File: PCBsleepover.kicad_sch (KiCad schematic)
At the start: 0 parts

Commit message: worked on sch
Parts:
- added BT1: Battery, symbol Device:Battery
- added C1: C_Polarized, symbol Device:C_Polarized
- added D1: LED, symbol Device:LED
- added R1, R2: R, symbol Device:R
- added R3: R_Variable, symbol Device:R_Variable
- added SW1: SW_Push, symbol Switch:SW_Push
- added U1: ICM7555xB, Package_SO:SOIC-8_3.9x4.9mm_P1.27mm, symbol Timer:ICM7555xB
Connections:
- new net: C1.1, R2.1, U1.2 (TRIG), U1.6 (THRES)
- new net: BT1.2 (-), SW1.2
- new net: R1.1, U1.3 (OUT)
- new net: R3.2, SW1.1, U1.4 (~{RST}), U1.8 (VCC)
- new net: R2.2, R3.1, U1.7 (DISCH)
- new net GND: BT1.1 (+), C1.2, D1.1 (K), U1.1 (GND)
- new net TOUT: D1.2 (A), R1.2
- no-connect marks 0 -> 1

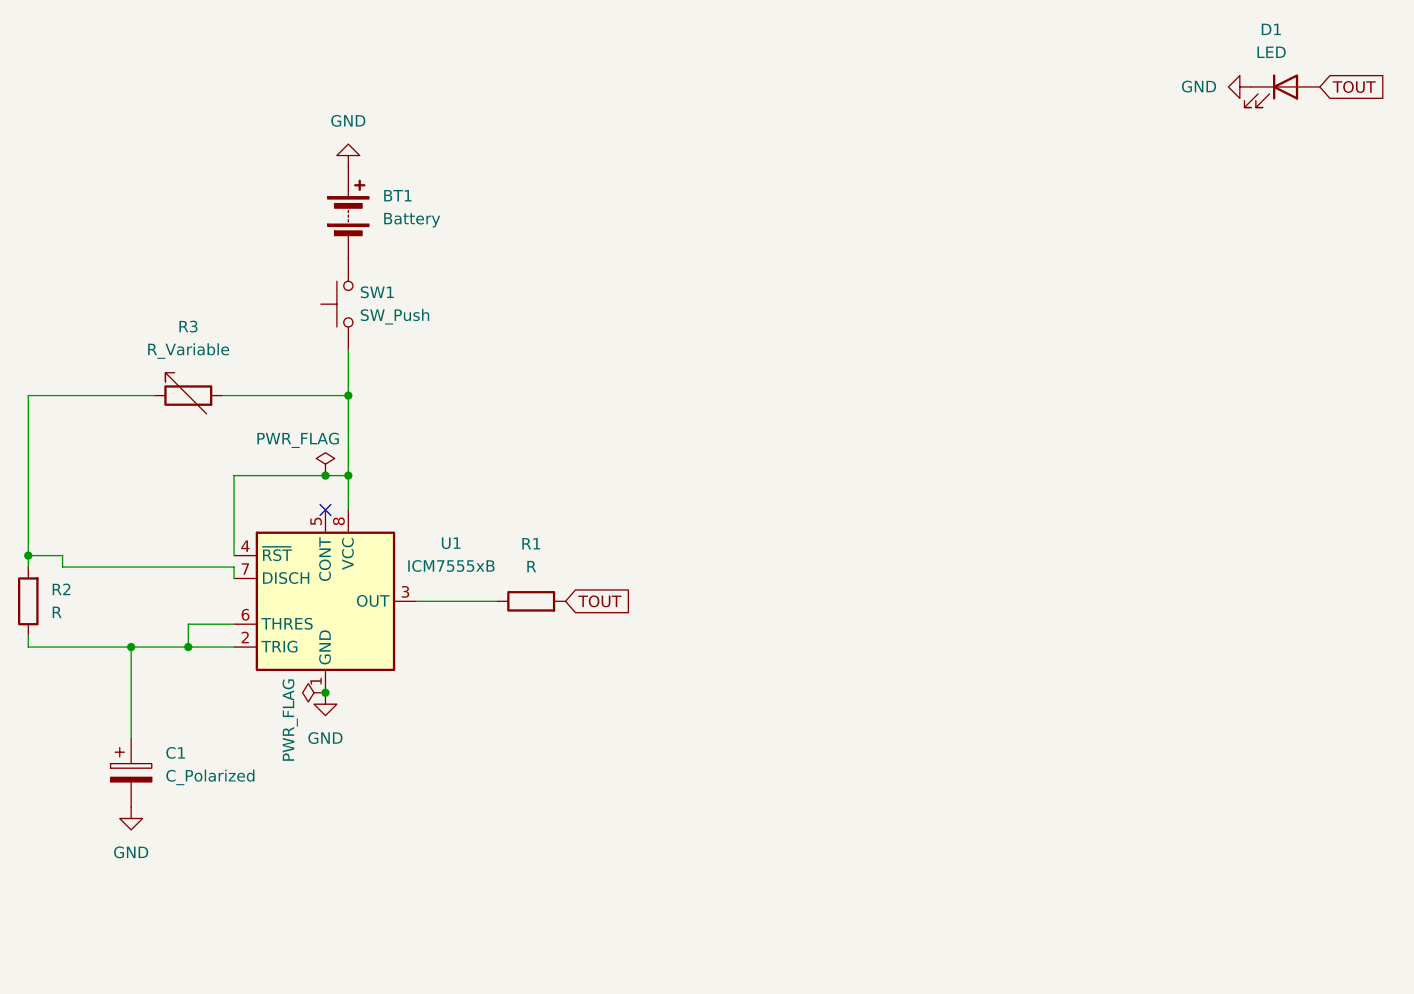
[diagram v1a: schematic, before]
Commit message: finished sch and added footprints and pcb
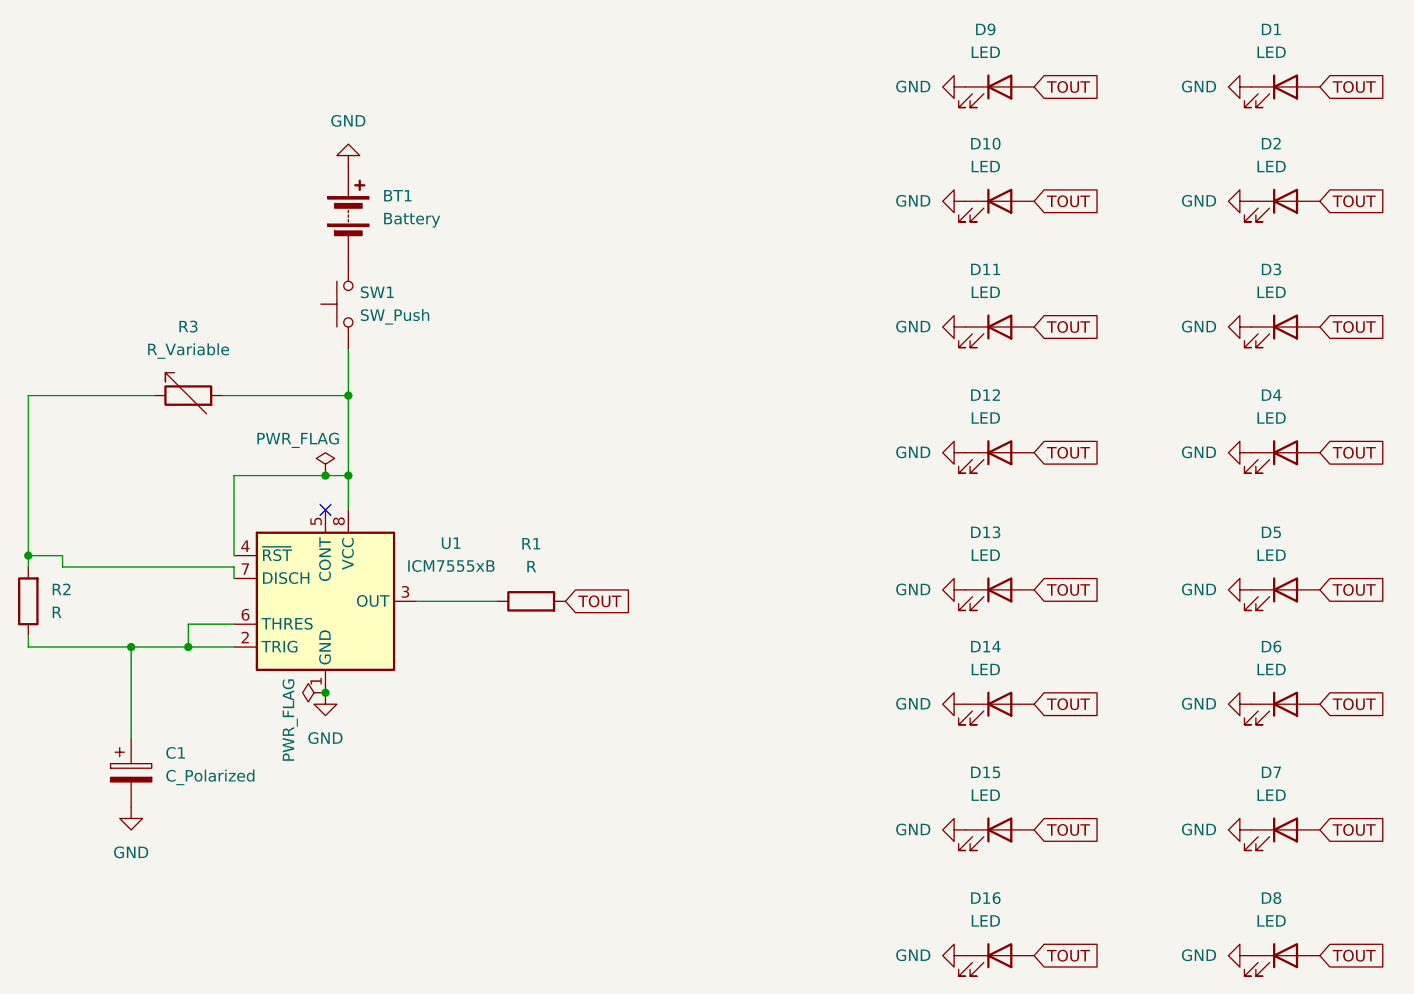
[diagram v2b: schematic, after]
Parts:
- added D10, D11, D12, D13, D14, D15, D16, D2, D3, D4, D5, D6, D7, D8, D9: LED, LED_THT:LED_D5.0mm, symbol Device:LED
- BT1: footprint (none) -> Connector_Wire:SolderWire-0.1sqmm_1x02_P3.6mm_D0.4mm_OD1mm
- C1: footprint (none) -> Capacitor_THT:CP_Radial_D5.0mm_P2.50mm
- D1: footprint (none) -> LED_THT:LED_D5.0mm
- R1, R2: footprint (none) -> Resistor_THT:R_Axial_DIN0207_L6.3mm_D2.5mm_P7.62mm_Horizontal
- R3: footprint (none) -> Potentiometer_THT:Potentiometer_Bourns_3386P_Vertical
- SW1: footprint (none) -> Button_Switch_THT:SW_PUSH_6mm
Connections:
- net GND: now also D10.1 (K), D11.1 (K), D12.1 (K), D13.1 (K), D14.1 (K), D15.1 (K), D16.1 (K), D2.1 (K), D3.1 (K), D4.1 (K), D5.1 (K), D6.1 (K), D7.1 (K), D8.1 (K), D9.1 (K)
- net TOUT: now also D10.2 (A), D11.2 (A), D12.2 (A), D13.2 (A), D14.2 (A), D15.2 (A), D16.2 (A), D2.2 (A), D3.2 (A), D4.2 (A), D5.2 (A), D6.2 (A), D7.2 (A), D8.2 (A), D9.2 (A)
